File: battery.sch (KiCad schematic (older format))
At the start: 45 parts, among them J1 MEGAFIT-4SKT, SW1 M2022LL2W13, SW2 M2022LL2W13, U1 VHE100W, U16 MCP601-SOT, U17 MCP601-SOT, U18 MCP601-SOT, U19 MCP601-SOT, U2 VHE100W, U4 INA139, U5 INA139, U6 INA139

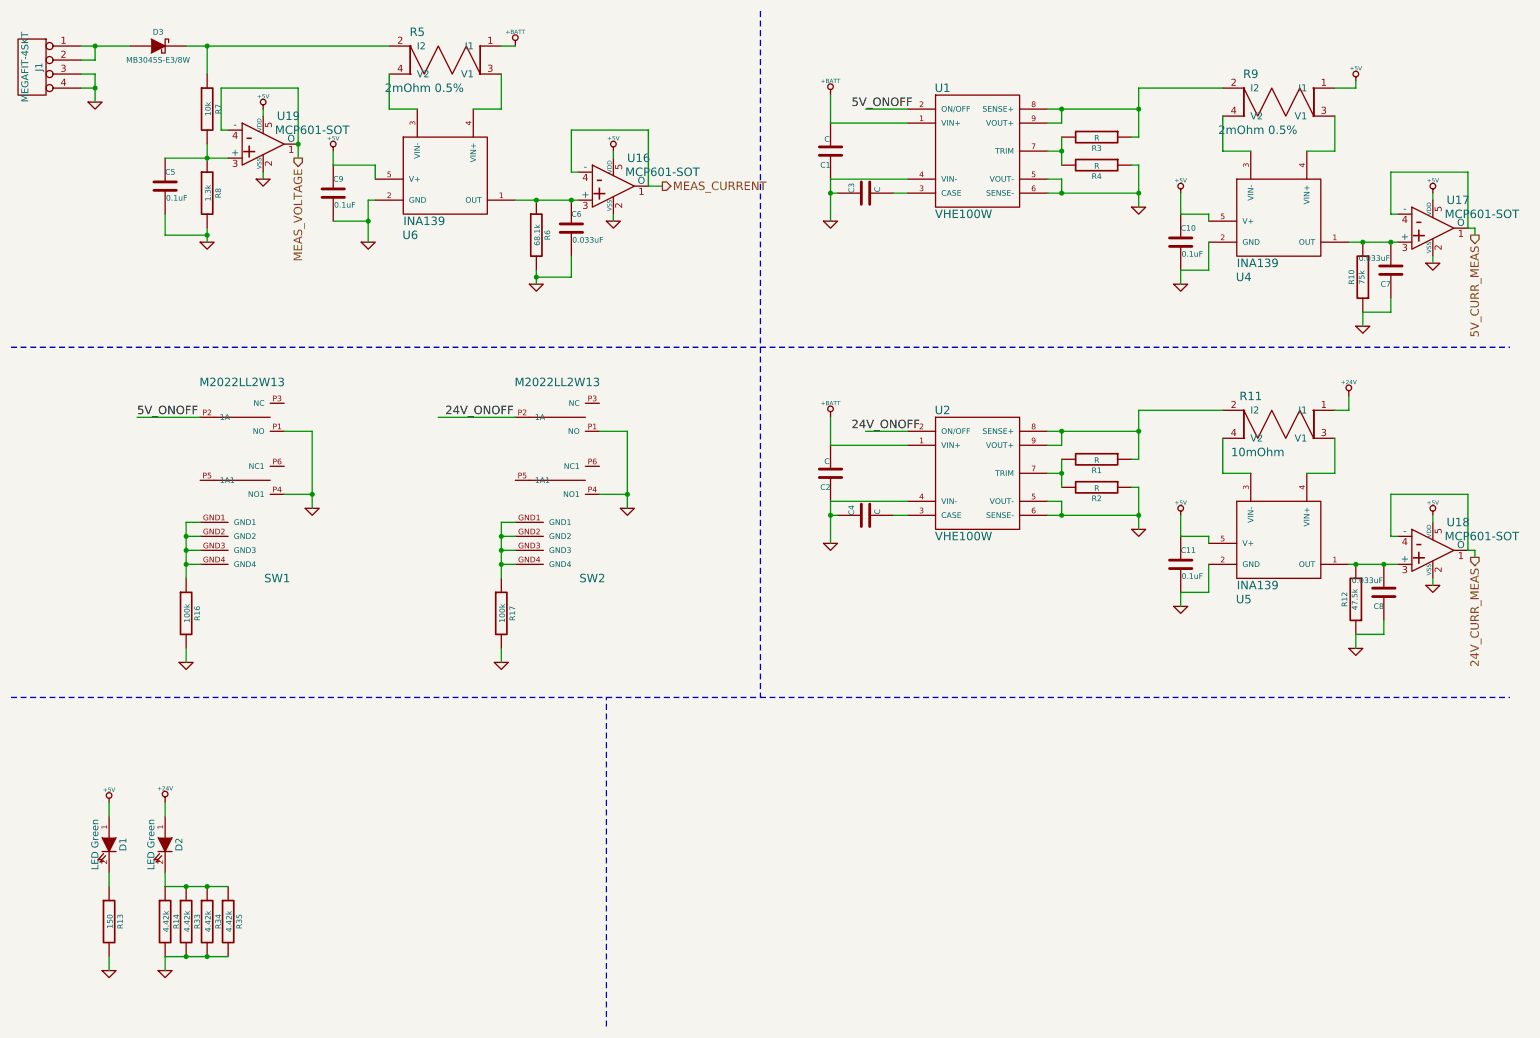
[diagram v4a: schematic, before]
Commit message: Updating design with new 12v bus.
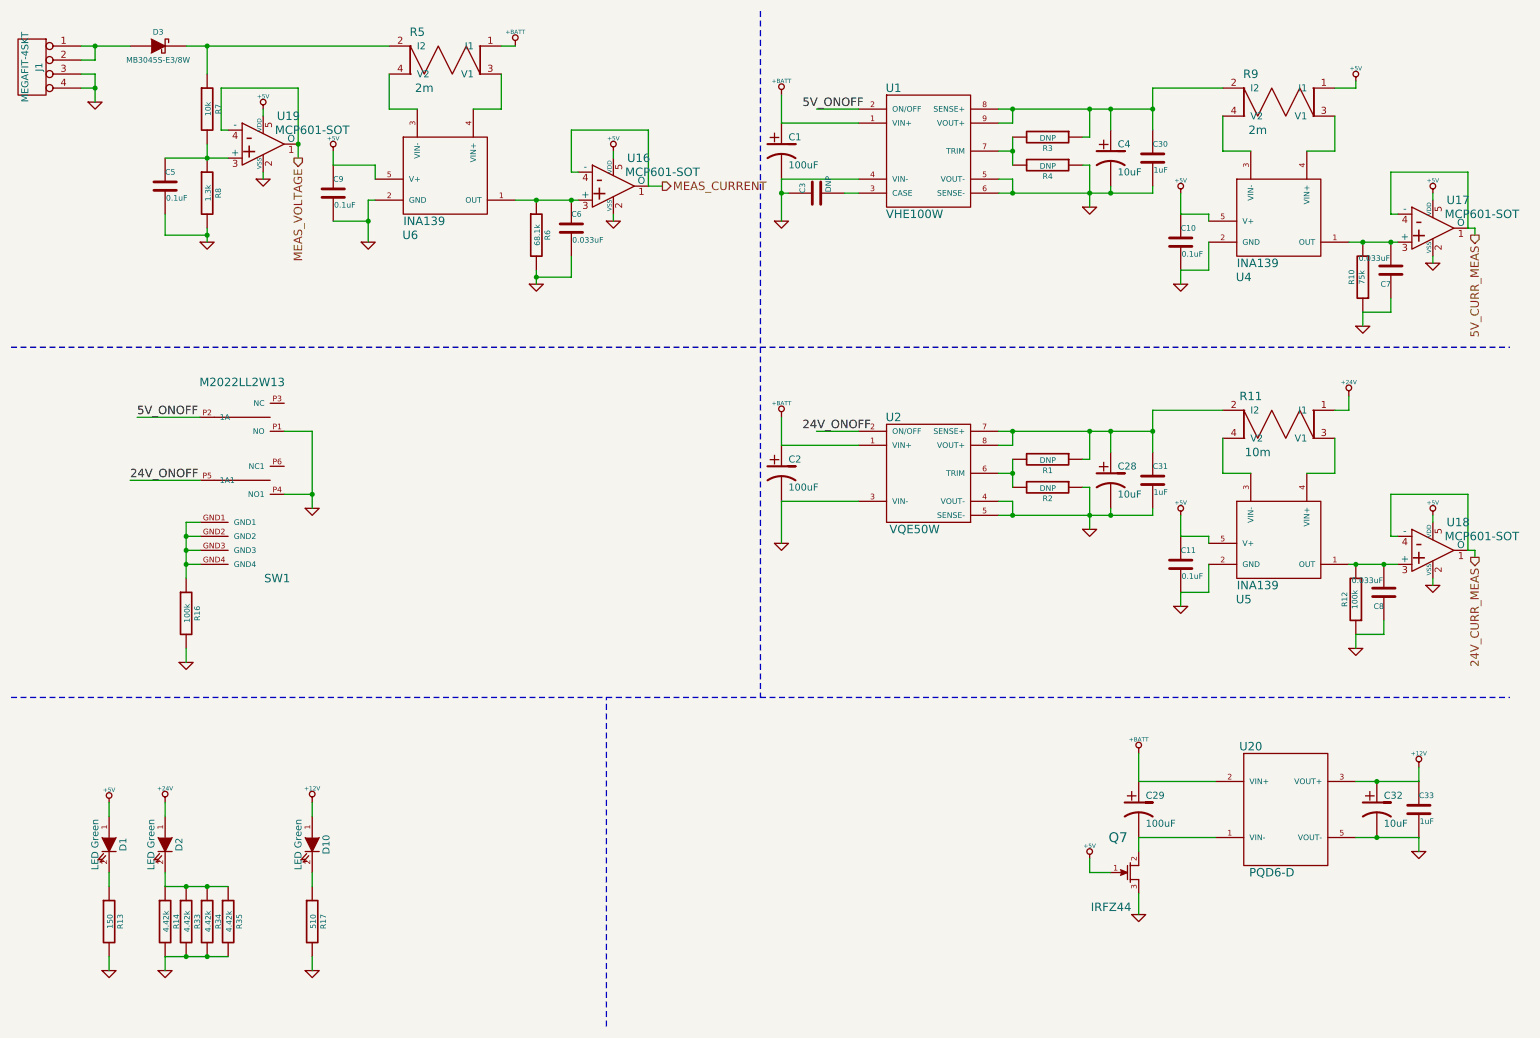
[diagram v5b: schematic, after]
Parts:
- removed C1, C2, C4: C, SM0805, symbol C
- removed SW2: M2022LL2W13, switch-M2022LL2W13, symbol M2022LL2W13
- removed U2: VHE100W, cui-VHE100W, symbol VHE100W
- added C1, C2, C29: 100uF, ~, symbol CP1
- added C28, C32, C4: 10uF, ~, symbol CP1
- added C30, C31, C33: 1uF, ~, symbol C
- added D10: LED Green, ~, symbol LED
- added Q7: IRFZ44, ~, symbol FET_N_GDS
- added U2: VQE50W, ~, symbol VQE50W
- added U20: PQD6-D, ~, symbol PQD6-D
- C3: value C -> DNP
- R1, R2, R3, R4: value R -> DNP
- R11: value 10mOhm -> 10m
- R12: value 47.5k -> 100k; Digikey P47.5KDACT-ND -> P100KCCT-ND
- R16: Digikey P100KACT-ND -> P100KCCT-ND
- R17: value 100k -> 510; Digikey P100KACT-ND -> P510FCT-ND
- R5, R9: value 2mOhm 0.5% -> 2m
- U1: footprint cui-VHE100W -> ~
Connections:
- net +5V: now also Q7.1 (G)
- net +BATT: now also C1.1, C2.1, C29.1, U2.1 (VIN+), U20.2 (VIN+)
- net 24V_ONOFF: now also SW1.P5 (1A1)
- net GND: now also C1.2, C2.2, C28.2, C30.2, C31.2, C32.2, C33.2, C4.2, Q7.3 (S), U2.3 (VIN-), U2.4 (VOUT-), U2.5 (SENSE-), U20.5 (VOUT-)
- net at R3.1, R9.2 (I2), U1.8 (SENSE+)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: now also C30.1, C4.1
- net at R17.1: now also D10.2 (K)
- net at R1.2, R2.2: now also U2.6 (TRIM)
- net at R1.1, R11.2 (I2): now also C28.1, C31.1, U2.7 (SENSE+), U2.8 (VOUT+)
- new net: C29.2, Q7.2 (D), U20.1 (VIN-)
- new net +12V: C32.1, C33.1, D10.1 (A), U20.3 (VOUT+)
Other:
- moved on the sheet: C3, R1, R2, R3, R4

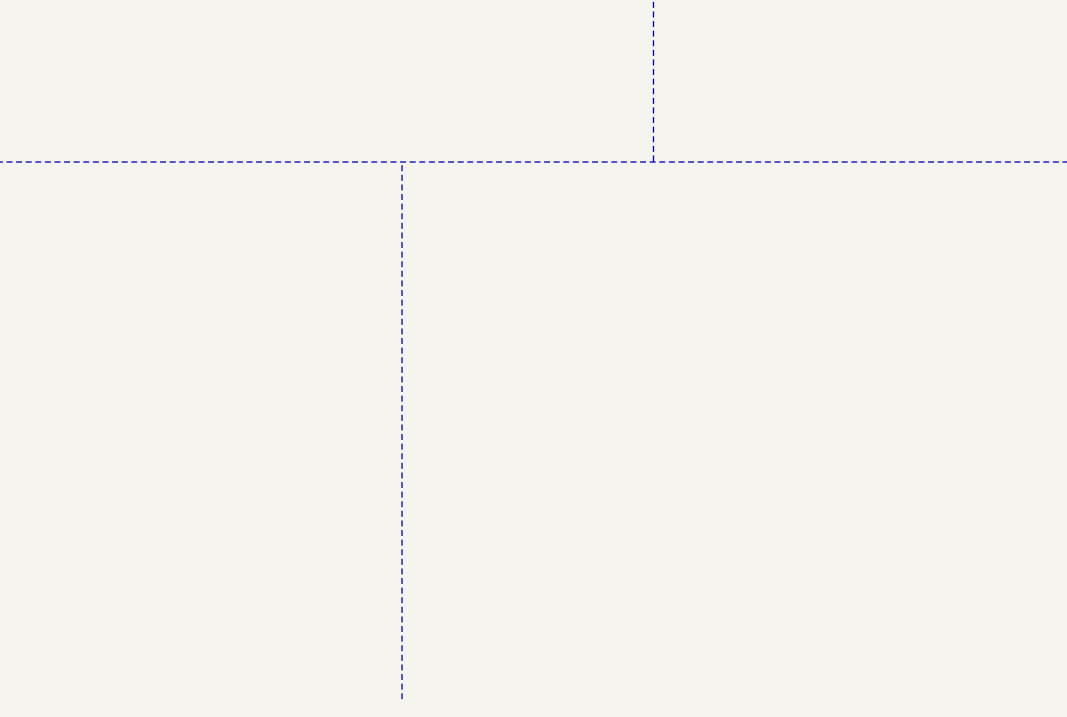
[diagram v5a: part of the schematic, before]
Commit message: Adding gps receiver, updating netlist and completing component assignment.
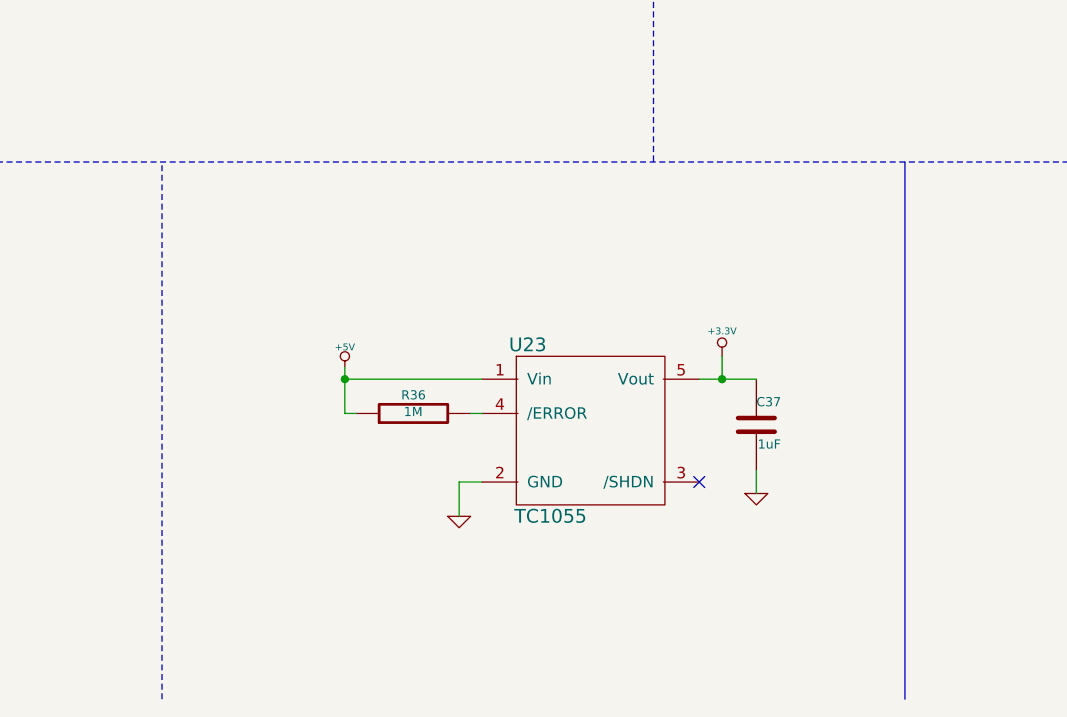
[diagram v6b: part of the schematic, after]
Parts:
- added C37: 1uF, ~, symbol C
- added R36: 1M, SM0805, symbol R
- added U23: TC1055, ~, symbol TC1055
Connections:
- net +5V: now also R36.1, U23.1 (Vin)
- net GND: now also C37.2, U23.2 (GND)
- new net: R36.2, U23.4 (/ERROR)
- new net +3.3V: C37.1, U23.5 (Vout)
- no-connect marks 0 -> 1
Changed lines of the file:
@@
 LIBS:w_analog
 LIBS:p_meas_spec
+LIBS:p_ublox
+LIBS:p_microchip
 LIBS:distro-cache
 EELAYER 27 0
@@
 Sheet 2 9
 Title ""
-Date "22 aug 2015"
+Date "24 aug 2015"
 Rev ""
 Comp ""
@@
 	500  5400 11200 5400
 Wire Notes Line
-	4750 7750 4750 5400
+	3700 7750 3700 5400
 Wire Wire Line
 	10050 2150 10400 2150
@@
 	1    0    0    -1
 $EndComp
+Wire Bus Line
+	6950 7750 6950 5400
+$Comp
+L TC1055 U23
+U 1 1 55DB7543
+P 5550 6600
+F 0 "U23" H 5300 7000 60  0000 C CNN
+F 1 "TC1055" H 5400 6250 60  0000 C CNN
+F 2 "~" H 5500 6650 60  0000 C CNN
+F 3 "~" H 5500 6650 60  0000 C CNN
+F 4 "TC10553.3VCT713CT-ND" H 5550 6600 60  0001 C CNN "Digikey"
+	1    5550 6600
+	1    0    0    -1
+$EndComp
+$Comp
+L GND #PWR042
+U 1 1 55DB7552
+P 5000 6950
+F 0 "#PWR042" H 5000 6950 30  0001 C CNN
+F 1 "GND" H 5000 6880 30  0001 C CNN
+F 2 "" H 5000 6950 60  0000 C CNN
+F 3 "" H 5000 6950 60  0000 C CNN
+	1    5000 6950
+	1    0    0    -1
+$EndComp
+$Comp
+L +5V #PWR043
+U 1 1 55DB755F
+P 4500 6300
+F 0 "#PWR043" H 4500 6390 20  0001 C CNN
+F 1 "+5V" H 4500 6390 30  0000 C CNN
+F 2 "" H 4500 6300 60  0000 C CNN
+F 3 "" H 4500 6300 60  0000 C CNN
+	1    4500 6300
+	1    0    0    -1
+$EndComp
+Wire Wire Line
+	5100 6800 5000 6800
+Wire Wire Line
+	5000 6800 5000 6950
+$Comp
+L R R36
+U 1 1 55DB7716
+P 4800 6500
+F 0 "R36" V 4880 6500 40  0000 C CNN
+F 1 "1M" V 4807 6501 40  0000 C CNN
+F 2 "SM0805" V 4730 6500 30  0001 C CNN
+F 3 "~" H 4800 6500 30  0000 C CNN
+F 4 "P1.00MCCT-ND" V 4800 6500 60  0001 C CNN "Digikey"
+	1    4800 6500
+	0    -1   -1   0
+$EndComp
+Wire Wire Line
+	4550 6500 4500 6500
+Wire Wire Line
+	4500 6500 4500 6300
+Wire Wire Line
+	5100 6350 4500 6350
+Connection ~ 4500 6350
+$Comp
+L +3.3V #PWR044
+U 1 1 55DB7900
+P 6150 6250
+F 0 "#PWR044" H 6150 6210 30  0001 C CNN
+F 1 "+3.3V" H 6150 6360 30  0000 C CNN
+F 2 "" H 6150 6250 60  0000 C CNN
+F 3 "" H 6150 6250 60  0000 C CNN
+	1    6150 6250
+	1    0    0    -1
+$EndComp
+Wire Wire Line
+	6050 6350 6300 6350
+Wire Wire Line
+	6150 6350 6150 6250
+NoConn ~ 6050 6800
+$Comp
+L C C37
+U 1 1 55DB7C96
+P 6300 6550
+F 0 "C37" H 6300 6650 40  0000 L CNN
+F 1 "1uF" H 6306 6465 40  0000 L CNN
+F 2 "~" H 6338 6400 30  0000 C CNN
+F 3 "~" H 6300 6550 60  0000 C CNN
+F 4 "399-8147-1-ND" H 6300 6550 60  0001 C CNN "Digikey"
+	1    6300 6550
+	1    0    0    -1
+$EndComp
+$Comp
+L GND #PWR045
+U 1 1 55DB7C9C
+P 6300 6850
+F 0 "#PWR045" H 6300 6850 30  0001 C CNN
+F 1 "GND" H 6300 6780 30  0001 C CNN
+F 2 "" H 6300 6850 60  0000 C CNN
+F 3 "" H 6300 6850 60  0000 C CNN
+	1    6300 6850
+	1    0    0    -1
+$EndComp
+Wire Wire Line
+	6300 6850 6300 6750
+Connection ~ 6150 6350
+Wire Wire Line
+	5050 6500 5100 6500
 $EndSCHEMATC

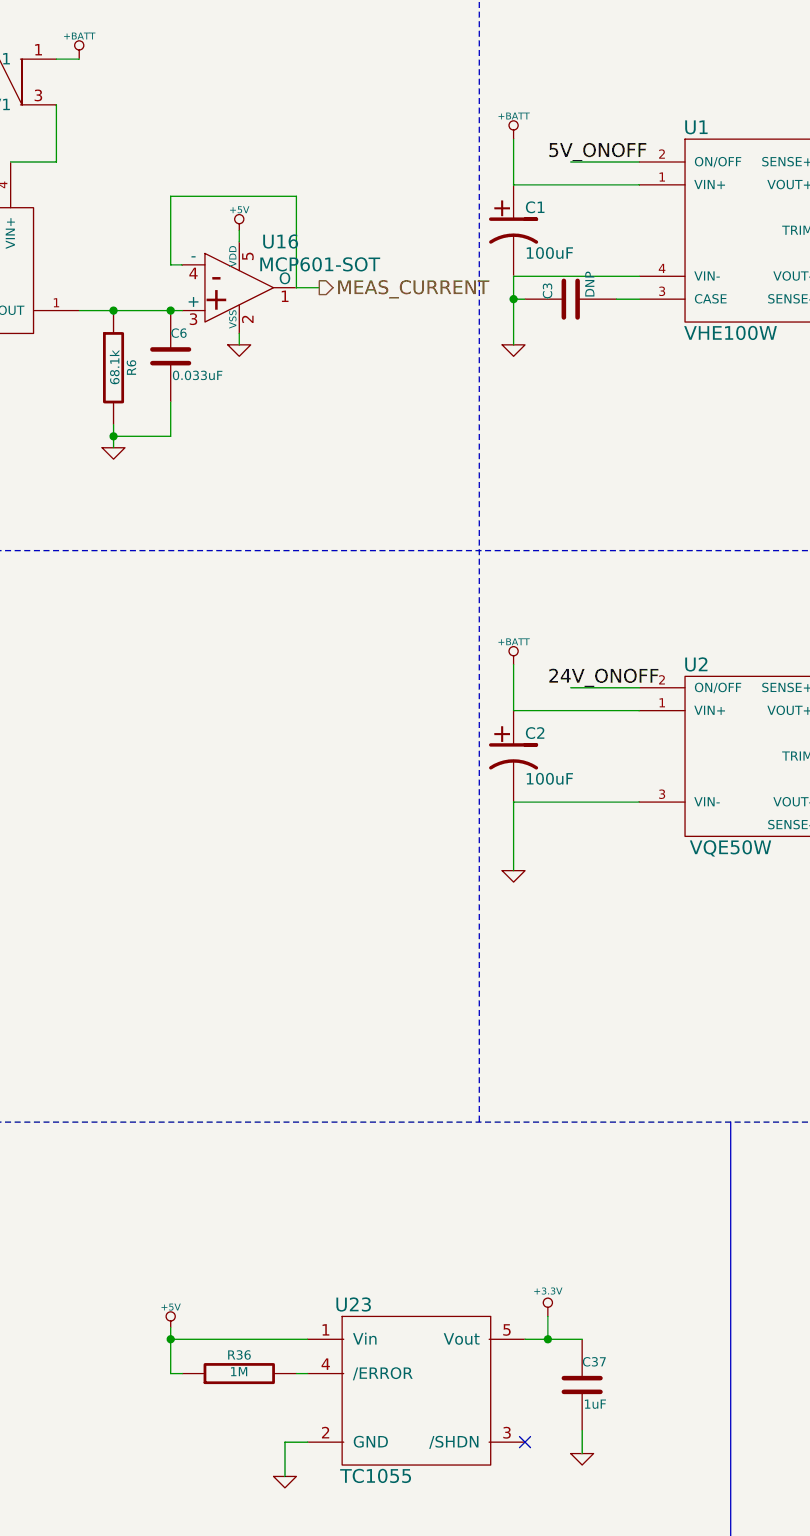
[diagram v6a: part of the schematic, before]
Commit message: Updating layout and component pad configs.
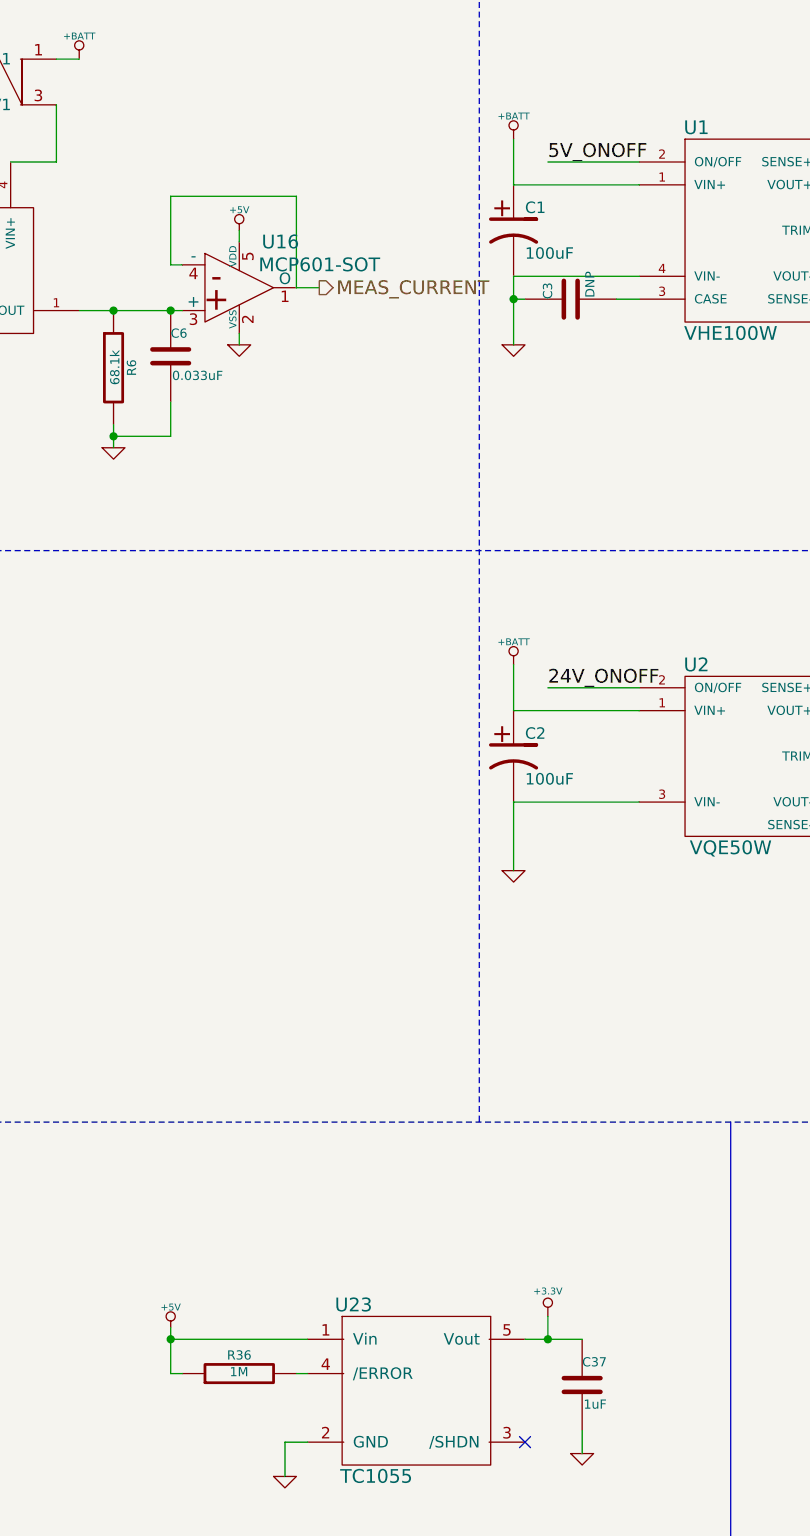
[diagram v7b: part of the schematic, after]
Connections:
- net 24V_ONOFF: now also U2.2 (ON/OFF)
- net 5V_ONOFF: now also U1.2 (ON/OFF)
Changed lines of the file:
@@
 Sheet 2 9
 Title ""
-Date "24 aug 2015"
+Date "25 aug 2015"
 Rev ""
 Comp ""
@@
 	10100 1050 10100 1000
 Wire Wire Line
-	6550 1200 6250 1200
+	6550 1200 6150 1200
 Wire Wire Line
 	6000 1300 6550 1300
@@
 	1750 5050 1750 5150
 Wire Wire Line
-	6550 3500 6250 3500
+	6550 3500 6150 3500
 Wire Wire Line
 	6000 3600 6550 3600
@@
 $EndComp
 Wire Wire Line
-	4550 6500 4500 6500
-Wire Wire Line
-	4500 6500 4500 6300
+	4500 6500 4550 6500
+Wire Wire Line
+	4500 6300 4500 6500
 Wire Wire Line
 	5100 6350 4500 6350
